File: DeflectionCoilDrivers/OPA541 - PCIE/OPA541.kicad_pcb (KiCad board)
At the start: 2 copper layers, 145.8 x 63.2 mm, 31 parts, among them J1 Conn_01x06_Socket, J2 Conn_Coaxial_Small, J3 Conn_Coaxial_Small, J4 Conn_Coaxial_Small, U1 OPA541AP

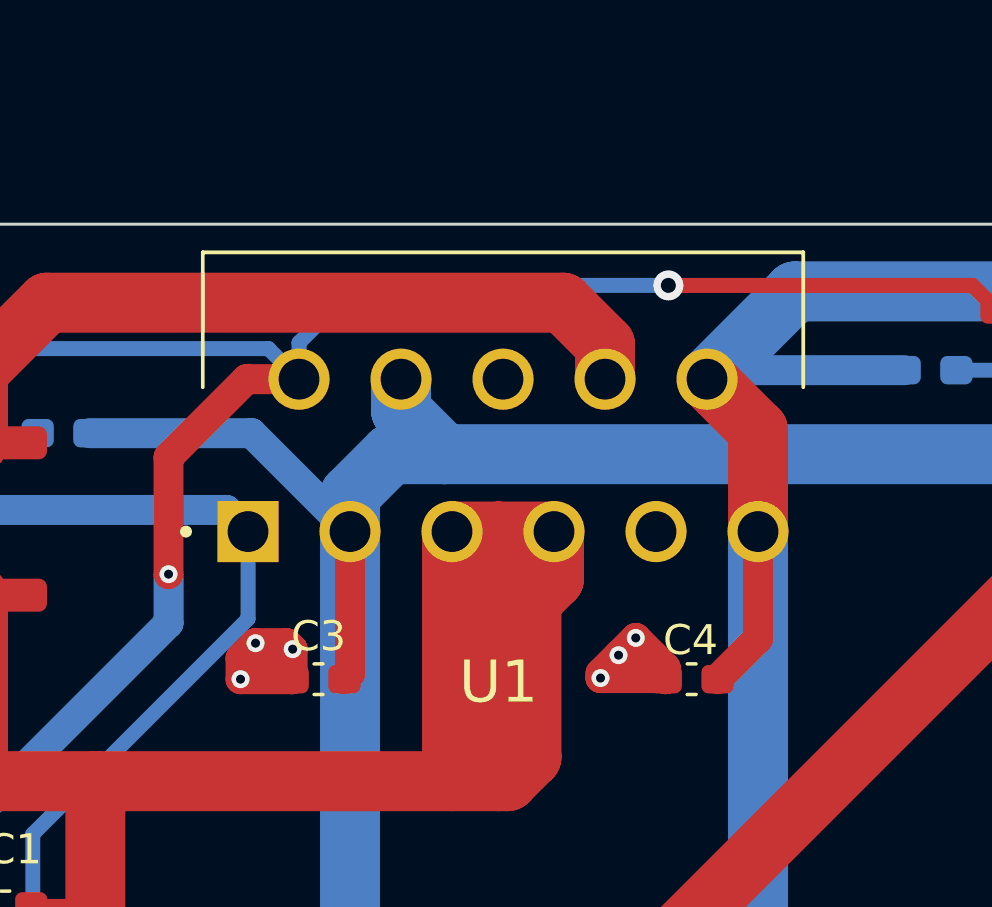
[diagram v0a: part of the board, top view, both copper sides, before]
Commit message: opa541 footprint update
moved opa541 footprint from snapmatic to kicad and custom symbol
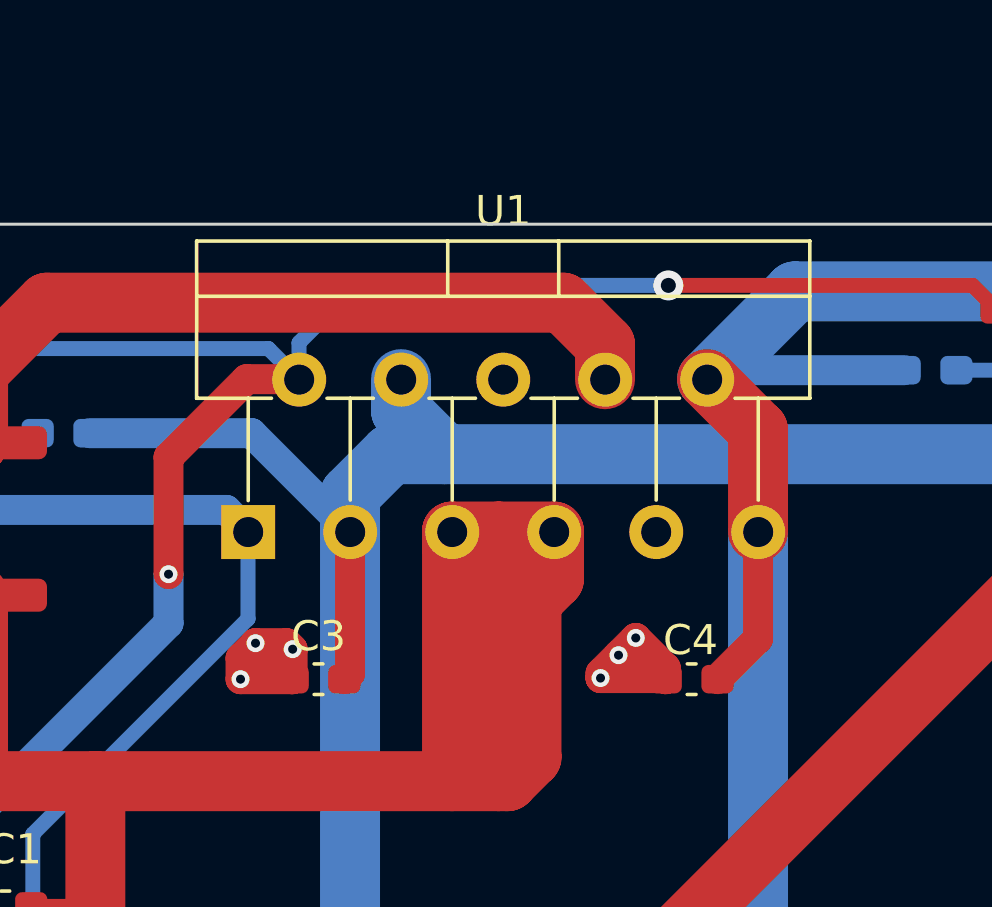
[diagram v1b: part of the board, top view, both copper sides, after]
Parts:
- U1: value OPA541AP -> ~; footprint Library:TO170P2027X462X2456-11 -> Package_TO_SOT_THT:TO-220-11_P3.4x5.08mm_StaggerOdd_Lead4.85mm_Vertical

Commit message: update
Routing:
- net Net-(J3-In): track 122.0 -> 134.2 mm
- net Net-(J3-Ext): track 159.6 -> 162.5 mm
- net -24V: track 190.0 -> 192.7 mm
- net Current_setpoint: track 127.3 -> 126.3 mm
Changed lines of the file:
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@@
 			(layers "*.Cu" "*.Mask")
 			(remove_unused_layers no)
-			(roundrect_rratio 0.138889)
+			(roundrect_rratio 0.1388888889)
 			(net 7 "+24V")
 			(pinfunction "Pin_1")
@@
 	)
 	(segment
-		(start 55.3615 130.326)
-		(end 74.7388 130.326)
+		(start 41.8084 143.764)
+		(end 70.2056 143.764)
 		(width 2)
 		(layer "F.Cu")
@@
 	)
 	(segment
-		(start 41.9235 143.764)
-		(end 55.3615 130.326)
-		(width 2)
-		(layer "F.Cu")
-		(net 1)
-	)
-	(segment
-		(start 41.8084 143.764)
-		(end 41.9235 143.764)
+		(start 108.7888 122.006)
+		(end 108.7888 123.576)
 		(width 2)
 		(layer "F.Cu")
@@
 	)
 	(segment
-		(start 108.7888 122.006)
-		(end 108.7888 123.576)
+		(start 70.2056 143.764)
+		(end 83.6436 130.326)
 		(width 2)
 		(layer "F.Cu")
@@
 	)
 	(segment
+		(start 83.6436 130.326)
+		(end 86.9442 130.326)
+		(width 2)
+		(layer "F.Cu")
+		(net 1)
+	)
+	(segment
 		(start 93.5 134.5)
 		(end 91.3625 134.5)
@@
 	)
 	(segment
-		(start 101.9888 136.2112)
-		(end 91.6928 146.5072)
+		(start 86.741 146.7358)
+		(end 84.917677 148.559123)
 		(width 2)
 		(layer "B.Cu")
@@
 	)
 	(segment
-		(start 84.917677 148.282323)
-		(end 84.917677 149.3)
-		(width 2)
-		(layer "B.Cu")
-		(net 4)
-	)
-	(segment
 		(start 101.9888 120.776)
 		(end 101.9888 122.006)
@@
 	)
 	(segment
-		(start 86.6928 146.5072)
-		(end 84.917677 148.282323)
+		(start 84.917677 148.559123)
+		(end 84.917677 149.3)
+		(width 2)
+		(layer "B.Cu")
+		(net 4)
+	)
+	(segment
+		(start 91.3638 146.7358)
+		(end 86.741 146.7358)
+		(width 2)
+		(layer "B.Cu")
+		(net 4)
+	)
+	(segment
+		(start 92.3544 147.7264)
+		(end 91.3638 146.7358)
 		(width 2)
 		(layer "B.Cu")
@@
 	)
 	(segment
-		(start 101.9888 122.006)
-		(end 101.9888 136.2112)
+		(start 101.9888 139.7684)
+		(end 94.0308 147.7264)
 		(width 2)
 		(layer "B.Cu")
@@
 	)
 	(segment
-		(start 166.77 139.23)
-		(end 165 139.23)
+		(start 94.0308 147.7264)
+		(end 92.3544 147.7264)
+		(width 2)
+		(layer "B.Cu")
+		(net 4)
+	)
+	(segment
+		(start 101.9888 122.006)
+		(end 101.9888 139.7684)
 		(width 2)
 		(layer "B.Cu")
@@
 	)
 	(segment
-		(start 91.6928 146.5072)
-		(end 86.6928 146.5072)
+		(start 166.77 139.23)
+		(end 165 139.23)
 		(width 2)
 		(layer "B.Cu")
@@
 	)
 	(segment
-		(start 36.7284 148.844)
-		(end 41.783 148.844)
+		(start 107.5436 140.7414)
+		(end 77.8383 140.7414)
 		(width 2)
 		(layer "F.Cu")
@@
 	)
 	(segment
-		(start 47.244 159.893)
-		(end 58.293 148.844)
+		(start 41.8084 146.304)
+		(end 72.2757 146.304)
 		(width 2)
 		(layer "F.Cu")
@@
 	)
 	(segment
-		(start 41.783 159.893)
-		(end 47.244 159.893)
+		(start 36.7284 148.844)
+		(end 41.783 148.844)
 		(width 2)
 		(layer "F.Cu")
@@
 	)
 	(segment
-		(start 41.783 148.844)
-		(end 58.293 148.844)
+		(start 61.1632 146.304)
+		(end 47.5742 159.893)
 		(width 2)
 		(layer "F.Cu")
@@
 	)
 	(segment
-		(start 66.3956 140.7414)
-		(end 58.293 148.844)
+		(start 77.8383 140.7414)
+		(end 72.2757 146.304)
 		(width 2)
 		(layer "F.Cu")
@@
 	)
 	(segment
-		(start 107.5436 140.7414)
-		(end 66.3956 140.7414)
+		(start 131.165 117.12)
+		(end 107.5436 140.7414)
 		(width 2)
 		(layer "F.Cu")
@@
 	(segment
 		(start 131.165 117.12)
-		(end 107.5436 140.7414)
-		(width 2)
-		(layer "F.Cu")
-		(net 9)
-	)
-	(segment
-		(start 131.165 117.12)
 		(end 143.2 117.12)
 		(width 2)
@@
 	)
 	(segment
+		(start 47.5742 159.893)
+		(end 41.783 159.893)
+		(width 2)
+		(layer "F.Cu")
+		(net 9)
+	)
+	(segment
 		(start 82.5478 138)
 		(end 82.5738 138.026)
@@
 	)
 	(segment
-		(start 94.234 164.435)
-		(end 112.014 164.435)
-		(width 0.5)
-		(layer "F.Cu")
-		(net 150)
-	)
-	(segment
-		(start 93.091 147.6756)
-		(end 93.091 157.4292)
+		(start 93.091 157.4292)
+		(end 99.314 163.6522)
 		(width 0.5)
 		(layer "F.Cu")
@@
 	)
 	(segment
-		(start 93.091 157.4292)
-		(end 99.314 163.6522)
+		(start 94.234 164.435)
+		(end 112.014 164.435)
 		(width 0.5)
 		(layer "F.Cu")
@@
 	)
 	(segment
-		(start 90.2462 144.8308)
-		(end 93.091 147.6756)
+		(start 93.091 146.1516)
+		(end 93.091 157.4292)
 		(width 0.5)
 		(layer "F.Cu")
@@
 	)
 	(via
-		(at 90.2462 144.8308)
+		(at 93.091 146.1516)
 		(size 0.6)
 		(drill 0.3)
@@
 	)
 	(segment
-		(start 91.4146 132.089539)
-		(end 98.5888 124.915339)
+		(start 98.5888 124.915339)
+		(end 98.5888 122.006)
 		(width 0.5)
 		(layer "B.Cu")
@@
 	)
 	(segment
-		(start 98.5888 122.006)
-		(end 97.8678 121.285)
-		(width 1)
+		(start 91.4146 132.089539)
+		(end 98.5888 124.915339)
+		(width 0.5)
 		(layer "B.Cu")
 		(net 150)
 	)
 	(segment
-		(start 48.0822 121.285)
-		(end 41.656 127.7112)
+		(start 98.5888 122.006)
+		(end 97.8678 121.285)
 		(width 1)
 		(layer "B.Cu")
@@
 	)
 	(segment
-		(start 91.4146 143.6624)
+		(start 91.4146 144.4752)
 		(end 91.4146 132.089539)
 		(width 0.5)
@@
 	)
 	(segment
-		(start 97.8678 121.285)
-		(end 48.0822 121.285)
+		(start 48.0822 121.285)
+		(end 41.656 127.7112)
 		(width 1)
 		(layer "B.Cu")
@@
 	)
 	(segment
-		(start 98.5888 124.915339)
-		(end 98.5888 122.006)
+		(start 93.091 146.1516)
+		(end 91.4146 144.4752)
 		(width 0.5)
 		(layer "B.Cu")
@@
 	)
 	(segment
-		(start 90.2462 144.8308)
-		(end 91.4146 143.6624)
-		(width 0.5)
+		(start 97.8678 121.285)
+		(end 48.0822 121.285)
+		(width 1)
 		(layer "B.Cu")
 		(net 150)

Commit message: minor changes
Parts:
- added R8: 1k, Capacitor_THT:C_Disc_D6.0mm_W2.5mm_P5.00mm, F.Cu at (123.5, 123.1)
- moved C6 0.91 mm to (89.0, 149.2)
- moved R7 0.91 mm to (79.9, 150.5)
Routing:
- net Net-(R2-Pad1): track 90.8 -> 99.4 mm
- net Net-(J3-Ext): track 162.5 -> 168.5 mm
- net GND: track 60.7 -> 63.4 mm
- net -24V: track 192.7 -> 191.5 mm
